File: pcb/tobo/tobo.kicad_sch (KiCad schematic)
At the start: 97 parts, among them J1 54548-2272, J2 Conn_01x02_Pin, J4 54548-2472, J5 Conn_01x09_Pin, J6 Conn_01x09_Pin, J7 Conn_01x09_Pin, J8 Hroparts Elec TYPE-C-31-M-12, U10 5015, U11 5015, U12 5015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

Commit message: PCB tweaks and prettification
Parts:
- C15, C16: footprint Capacitor_THT:C_Disc_D5.0mm_W2.5mm_P2.50mm -> tobo-footprints:C_Disc_D5.0mm_W2.5mm_P2.50mm
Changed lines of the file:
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@@
 			)
 		)
-		(property "Footprint" "Capacitor_THT:C_Disc_D5.0mm_W2.5mm_P2.50mm"
+		(property "Footprint" "tobo-footprints:C_Disc_D5.0mm_W2.5mm_P2.50mm"
 			(at 213.36 88.9 0)
 			(effects
@@
 			)
 		)
-		(property "Footprint" "Capacitor_THT:C_Disc_D5.0mm_W2.5mm_P2.50mm"
+		(property "Footprint" "tobo-footprints:C_Disc_D5.0mm_W2.5mm_P2.50mm"
 			(at 215.9 91.44 0)
 			(effects

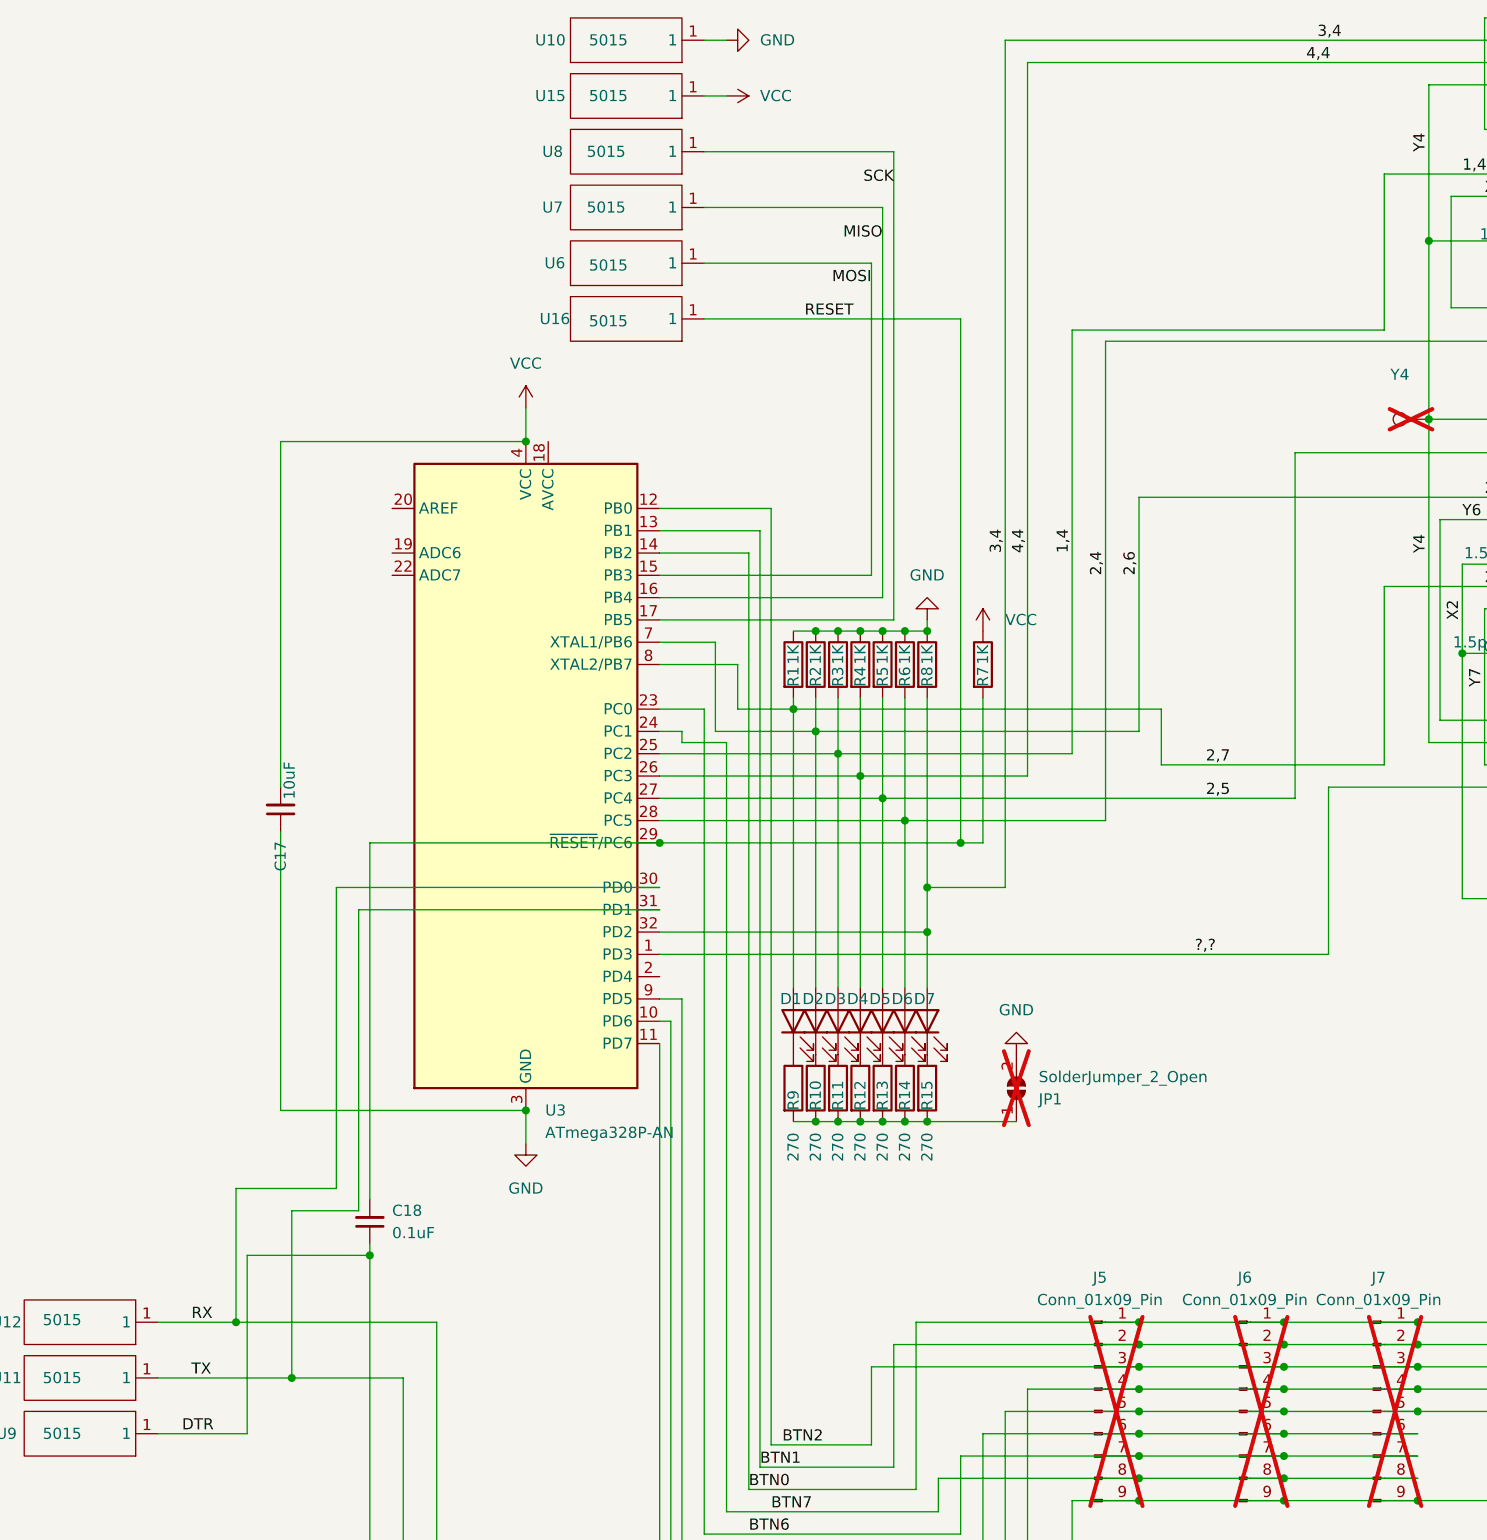
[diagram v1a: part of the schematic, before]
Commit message: Added missing pull-up for previously unused control channel
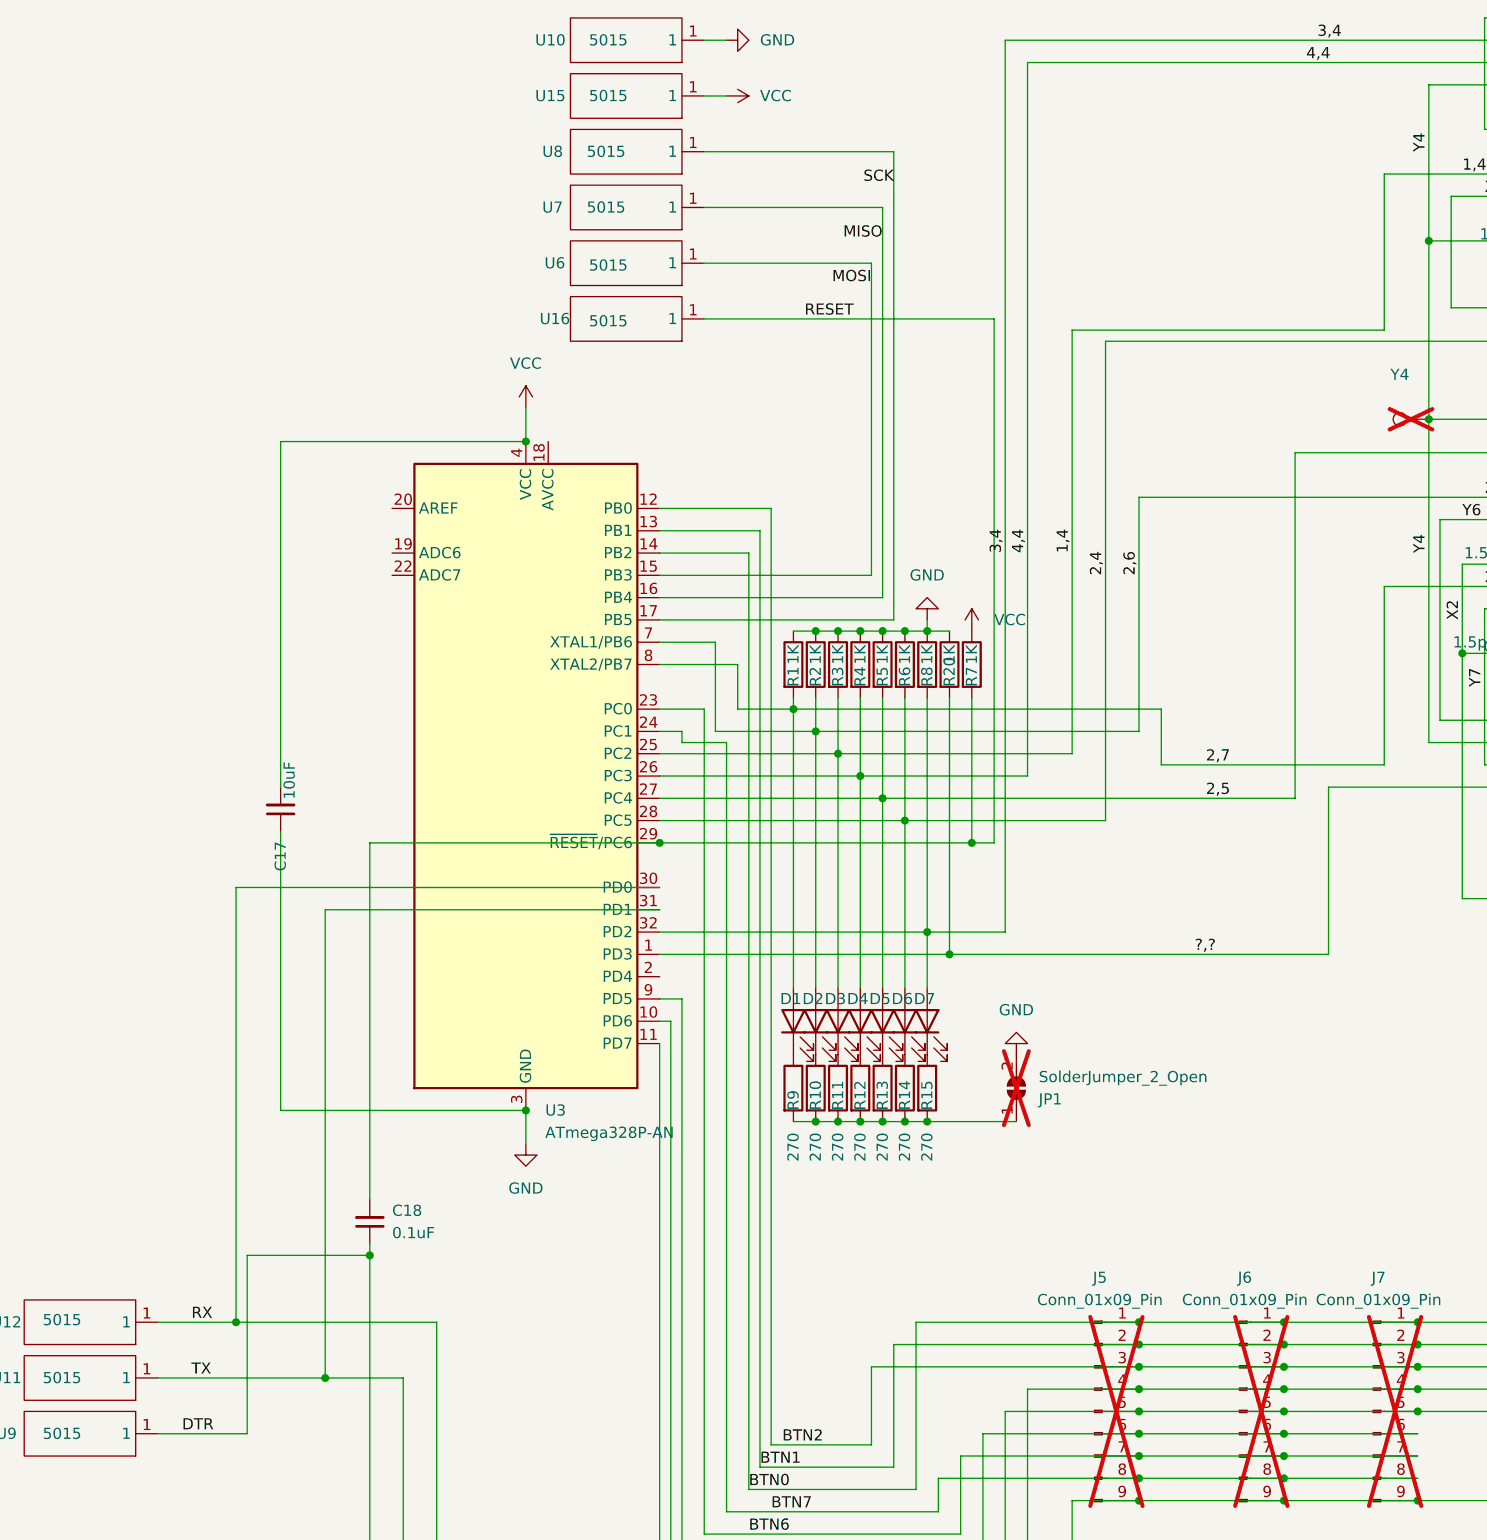
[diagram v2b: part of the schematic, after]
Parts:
- added R20: 1K, Resistor_SMD:R_0201_0603Metric, symbol Device:R
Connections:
- net ?,?: now also R20.2
- net GND: now also R20.1
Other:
- moved on the sheet: R7

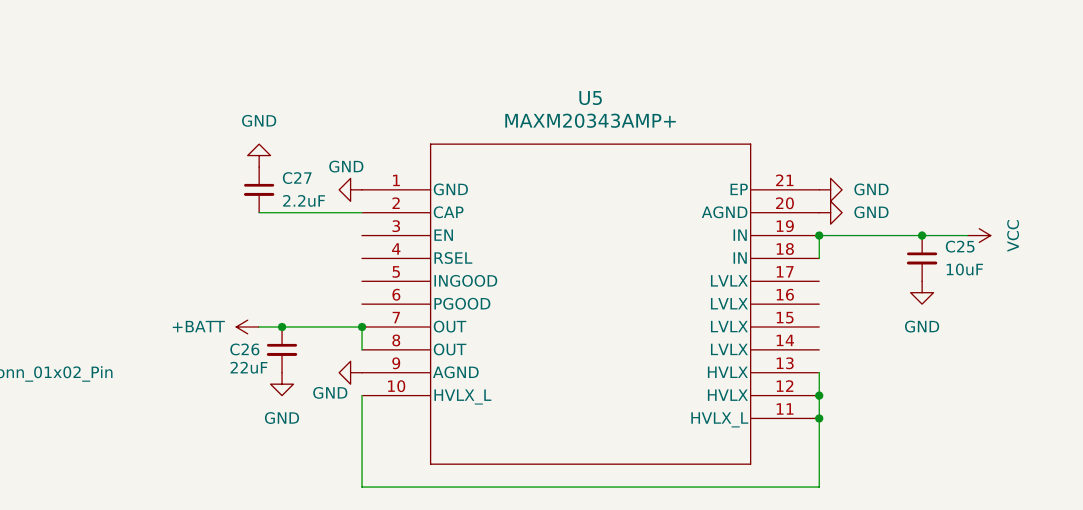
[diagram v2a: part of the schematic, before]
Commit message: Hooked the voltage converter up the right way around. Good catch!
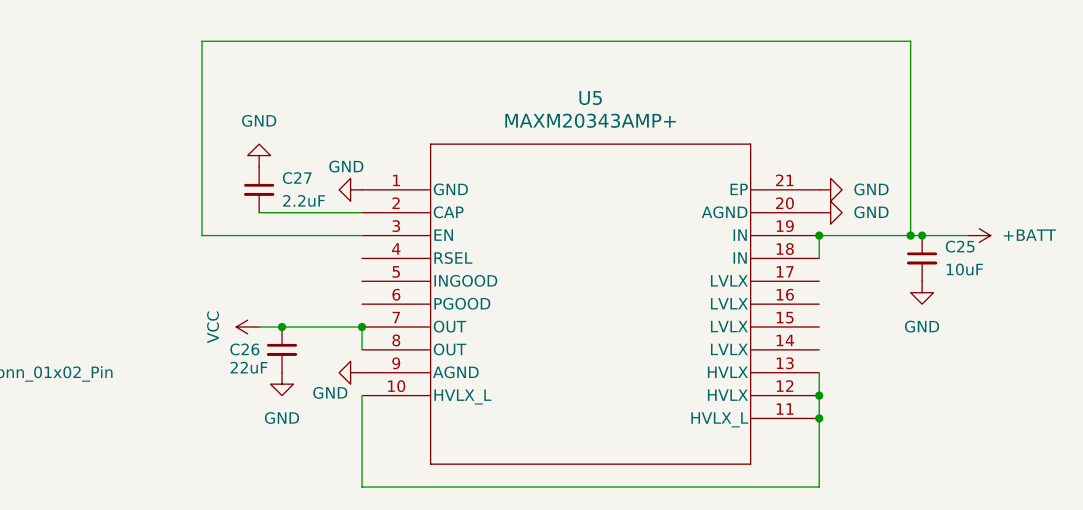
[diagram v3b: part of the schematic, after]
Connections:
- net +BATT: now also C25.1, U5.18 (IN), U5.19 (IN), U5.3 (EN); no longer C26.1, U5.7 (OUT), U5.8 (OUT)
- net VCC: now also C26.1, U5.7 (OUT), U5.8 (OUT); no longer C25.1, U5.18 (IN), U5.19 (IN)
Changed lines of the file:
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@@
 	)
 	(junction
+		(at 391.16 40.64)
+		(diameter 0)
+		(color 0 0 0 0)
+	)
+	(junction
 		(at 215.9 83.82)
 		(diameter 0)
@@
 	(wire
 		(pts
+			(xy 391.16 40.64) (xy 392.43 40.64)
+		)
+		(stroke
+			(width 0)
+			(type default)
+		)
+	)
+	(wire
+		(pts
 			(xy 193.04 83.82) (xy 194.31 83.82)
 		)
@@
 	(wire
 		(pts
+			(xy 312.42 19.05) (xy 391.16 19.05)
+		)
+		(stroke
+			(width 0)
+			(type default)
+		)
+	)
+	(wire
+		(pts
 			(xy 90.17 74.93) (xy 101.6 74.93)
 		)
@@
 	(wire
 		(pts
+			(xy 312.42 40.64) (xy 312.42 19.05)
+		)
+		(stroke
+			(width 0)
+			(type default)
+		)
+	)
+	(wire
+		(pts
 			(xy 226.06 19.05) (xy 226.06 29.21)
 		)
@@
 	(wire
 		(pts
+			(xy 330.2 40.64) (xy 312.42 40.64)
+		)
+		(stroke
+			(width 0)
+			(type default)
+		)
+	)
+	(wire
+		(pts
 			(xy 184.15 83.82) (xy 187.96 83.82)
 		)
@@
 	(wire
 		(pts
-			(xy 381 40.64) (xy 392.43 40.64)
+			(xy 381 40.64) (xy 391.16 40.64)
 		)
 		(stroke
@@
 	(wire
 		(pts
+			(xy 391.16 19.05) (xy 391.16 40.64)
+		)
+		(stroke
+			(width 0)
+			(type default)
+		)
+	)
+	(wire
+		(pts
 			(xy 137.16 185.42) (xy 144.78 185.42)
 		)
@@
 	(symbol
 		(lib_id "power:+BATT")
-		(at 397.51 40.64 270)
+		(at 318.77 50.8 90)
 		(mirror x)
 		(unit 1)
@@
 		(dnp no)
 		(property "Reference" "#PWR033"
-			(at 393.7 40.64 0)
+			(at 322.58 50.8 0)
 			(effects
 				(font
@@
 		)
 		(property "Value" "VCC"
-			(at 402.59 40.64 0)
+			(at 313.69 50.8 0)
 			(effects
 				(font
@@
 		)
 		(property "Footprint" ""
-			(at 397.51 40.64 0)
+			(at 318.77 50.8 0)
 			(effects
 				(font
@@
 		)
 		(property "Datasheet" ""
-			(at 397.51 40.64 0)
+			(at 318.77 50.8 0)
 			(effects
 				(font
@@
 		)
 		(property "Description" "Power symbol creates a global label with name \"+BATT\""
-			(at 397.51 40.64 0)
+			(at 318.77 50.8 0)
 			(effects
 				(font
@@
 	(symbol
 		(lib_id "power:+BATT")
-		(at 318.77 50.8 90)
+		(at 397.51 40.64 270)
 		(unit 1)
 		(exclude_from_sim no)
@@
 		(fields_autoplaced yes)
 		(property "Reference" "#PWR032"
-			(at 322.58 50.8 0)
+			(at 393.7 40.64 0)
 			(effects
 				(font
@@
 		)
 		(property "Value" "+BATT"
-			(at 314.96 50.7999 90)
+			(at 401.32 40.6399 90)
 			(effects
 				(font
@@
 		)
 		(property "Footprint" ""
-			(at 318.77 50.8 0)
+			(at 397.51 40.64 0)
 			(effects
 				(font
@@
 		)
 		(property "Datasheet" ""
-			(at 318.77 50.8 0)
+			(at 397.51 40.64 0)
 			(effects
 				(font
@@
 		)
 		(property "Description" "Power symbol creates a global label with name \"+BATT\""
-			(at 318.77 50.8 0)
+			(at 397.51 40.64 0)
 			(effects
 				(font
